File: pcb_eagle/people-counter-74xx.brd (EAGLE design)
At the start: 30.5 x 68.2 mm, 13 parts, among them IC1 74LS90N, IC2 74LS47N

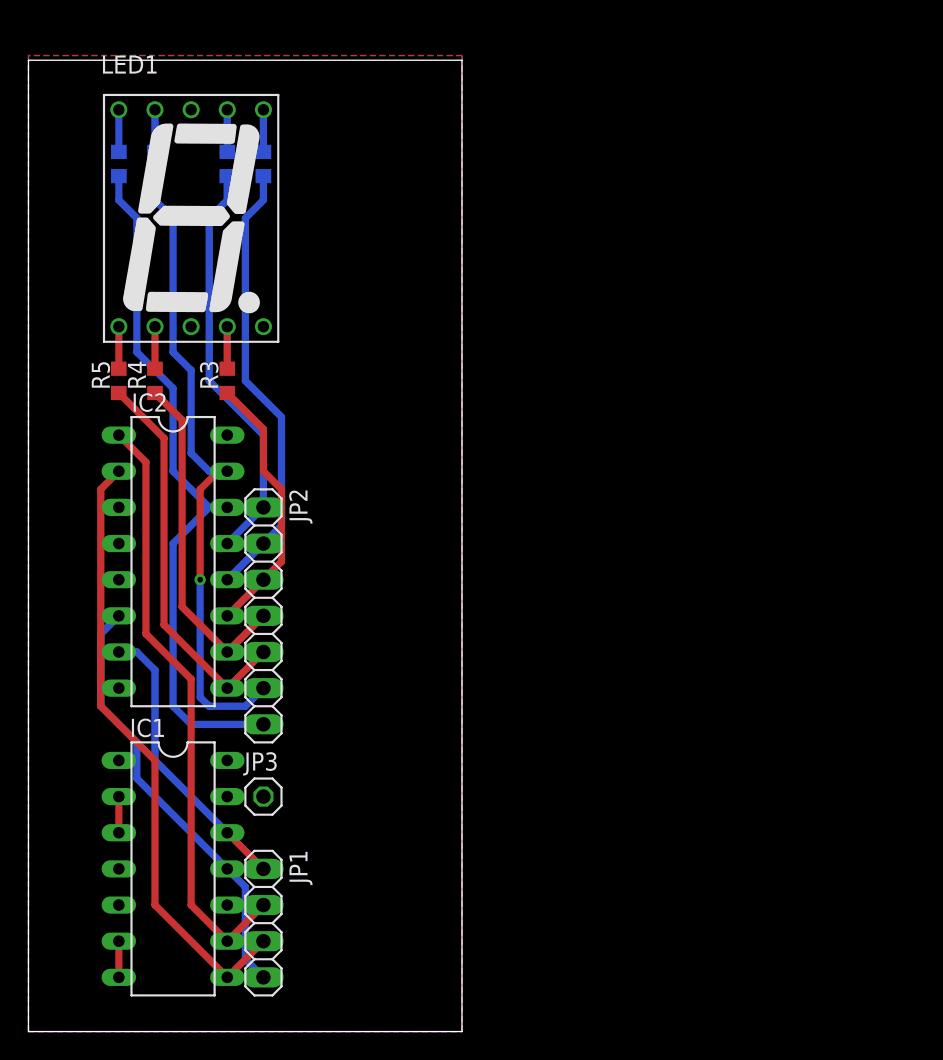
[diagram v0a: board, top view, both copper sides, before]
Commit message: PCB_EAGLE: finish layout of 4 design module (LED segment counter}
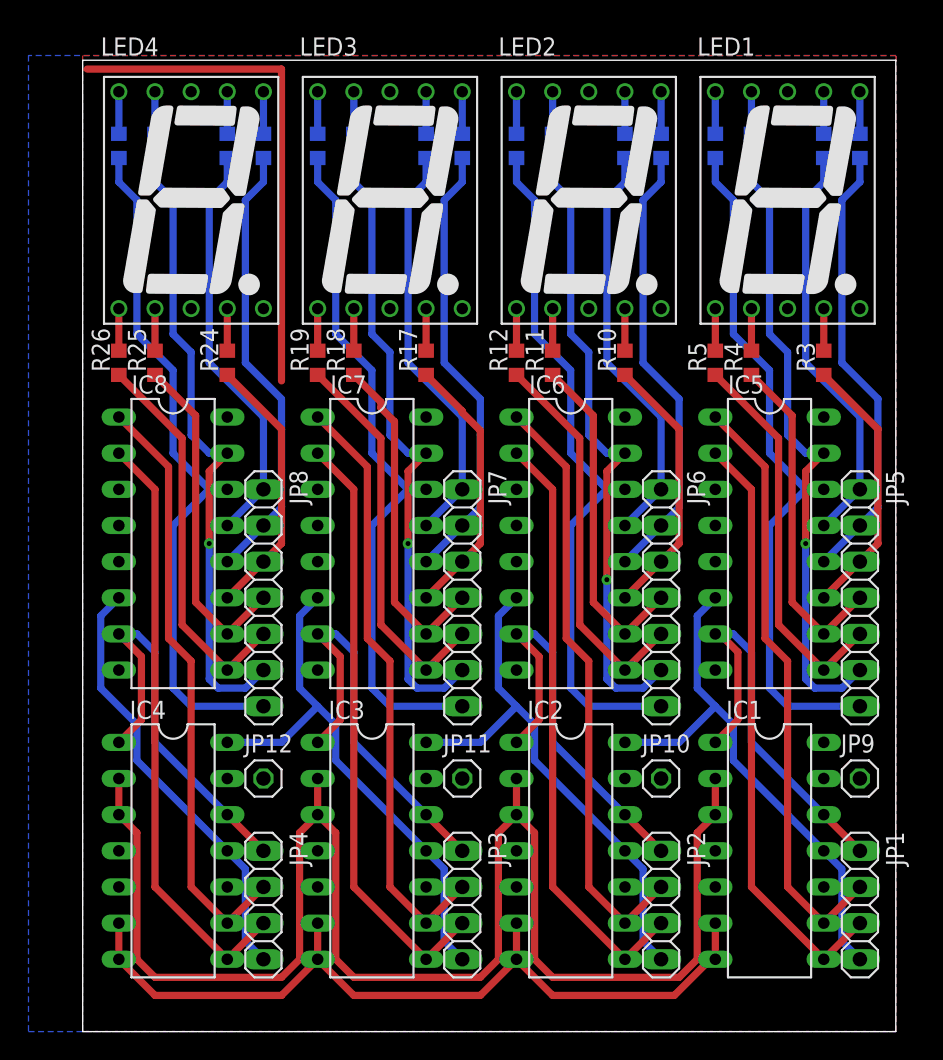
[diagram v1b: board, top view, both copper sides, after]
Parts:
- added IC3, IC4: 74LS90N, 74xx-eu:DIL14
- added IC5, IC6, IC7, IC8: 74LS47N, 74xx-eu:DIL16
- added JP10, JP11, JP12, JP9: GND, pinhead:1X01
- added JP4: NUM4, pinhead:1X04
- added JP5: DIG1, pinhead:1X07
- added JP6: DIG2, pinhead:1X07
- added JP7: DIG3, pinhead:1X07
- added JP8: DIG4, pinhead:1X07
- added LED2, LED3, LED4: 7-SEG_SA52-11, display-kingbright:SA52-11
- added R10, R11, R12, R13, R14, R15, R16, R17, R18, R19, R20, R21, R22, R23, R24, R25, R26, R27, R28, R8, R9: 220R, rcl:R0603
- IC2: value 74LS47N -> 74LS90N; device 74xx-eu:DIL16 -> 74xx-eu:DIL14
- JP2: value DIG1 -> NUM2; device pinhead:1X07 -> pinhead:1X04
- JP3: value GND -> NUM3; device pinhead:1X01 -> pinhead:1X04
- moved LED1 41.9 mm to (53.3, 58.4)
- moved R1 41.9 mm to (55.9, 62.2)
- moved R3 41.9 mm to (55.9, 47.0)
- moved IC1 41.9 mm to (52.1, 12.7)
- moved JP1 41.9 mm to (58.4, 8.89)
- moved R2 41.9 mm to (58.4, 62.2)
- moved R4 41.9 mm to (50.8, 47.0)
- moved R5 41.9 mm to (48.3, 47.0)
- moved R6 41.9 mm to (50.8, 62.2)
- moved R7 41.9 mm to (48.3, 62.2)
- moved IC2 34.5 mm to (38.1, 12.7)
- moved JP2 34.5 mm to (44.5, 8.89)
- moved JP3 15.9 mm to (30.5, 8.89), turned to 270 degrees
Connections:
- removed net CKB_DIG1: IC1.1
- removed net R0_DIG1: IC1.2, IC1.3
- removed net R9_DIG1: IC1.6, IC1.7
- new net A_DIG2: IC6.13, JP6.1, R8.1
- new net A_DIG3: IC7.13, JP7.1, R15.1
- new net A_DIG4: IC8.13, JP8.1, R22.1
- new net A_DIG_2: LED2.7, R8.2
- new net A_DIG_3: LED3.7, R15.2
- new net A_DIG_4: LED4.7, R22.2
- new net B_DIG2: IC6.12, JP6.2, R9.1
- new net B_DIG3: IC7.12, JP7.2, R16.1
- new net B_DIG4: IC8.12, JP8.2, R23.1
- new net B_DIG_2: LED2.6, R9.2
- new net B_DIG_3: LED3.6, R16.2
- new net B_DIG_4: LED4.6, R23.2
- new net C_DIG2: IC6.11, JP6.3, R10.1
- new net C_DIG3: IC7.11, JP7.3, R17.1
- new net C_DIG4: IC8.11, JP8.3, R24.1
- new net C_DIG_2: LED2.4, R10.2
- new net C_DIG_3: LED3.4, R17.2
- new net C_DIG_4: LED4.4, R24.2
- new net D_DIG2: IC6.10, JP6.4, R11.1
- new net D_DIG3: IC7.10, JP7.4, R18.1
- new net D_DIG4: IC8.10, JP8.4, R25.1
- new net D_DIG_2: LED2.2, R11.2
- new net D_DIG_3: LED3.2, R18.2
- new net D_DIG_4: LED4.2, R25.2
- new net E_DIG2: IC6.9, JP6.5, R12.1
- new net E_DIG3: IC7.9, JP7.5, R19.1
- new net E_DIG4: IC8.9, JP8.5, R26.1
- new net E_DIG_2: LED2.1, R12.2
- new net E_DIG_3: LED3.1, R19.2
- new net E_DIG_4: LED4.1, R26.2
- new net F_DIG2: IC6.15, JP6.6, R13.1
- new net F_DIG3: IC7.15, JP7.6, R20.1
- new net F_DIG4: IC8.15, JP8.6, R27.1
- new net F_DIG_2: LED2.9, R13.2
- new net F_DIG_3: LED3.9, R20.2
- new net F_DIG_4: LED4.9, R27.2
- new net G_DIG2: IC6.14, JP6.7, R14.1
- new net G_DIG3: IC7.14, JP7.7, R21.1
- new net G_DIG4: IC8.14, JP8.7, R28.1
- new net G_DIG_2: LED2.10, R14.2
- new net G_DIG_3: LED3.10, R21.2
- new net G_DIG_4: LED4.10, R28.2
- new net QA_IA_DIG2: IC2.1, IC2.12, IC6.7, JP2.1
- new net QA_IA_DIG3: IC3.1, IC3.12, IC7.7, JP3.1
- new net QA_IA_DIG4: IC4.1, IC4.12, IC8.7, JP4.1
- new net QB_IB_DIG2: IC2.9, IC6.1, JP2.2
- new net QB_IB_DIG3: IC3.9, IC7.1, JP3.2
- new net QB_IB_DIG4: IC4.9, IC8.1, JP4.2
- new net QC_IC_DIG2: IC2.8, IC6.2, JP2.3
- new net QC_IC_DIG3: IC3.8, IC7.2, JP3.3
- new net QC_IC_DIG4: IC4.8, IC8.2, JP4.3
- new net QD_ID_DIG2: IC2.11, IC3.14, IC6.6, JP2.4
- new net QD_ID_DIG3: IC3.11, IC4.14, IC7.6, JP3.4
- new net QD_ID_DIG4: IC4.11, IC8.6, JP4.4
- new net R0_DIG: IC1.2, IC1.3, IC2.2, IC2.3, IC3.2, IC3.3, IC4.2, IC4.3
- new net R9_DIG: IC1.6, IC1.7, IC2.6, IC2.7, IC3.6, IC3.7, IC4.6, IC4.7
- net A_DIG1: now also IC5.13, JP5.1; no longer IC2.13, JP2.1
- net B_DIG1: now also IC5.12, JP5.2; no longer IC2.12, JP2.2
- net C_DIG1: now also IC5.11, JP5.3; no longer IC2.11, JP2.3
- net D_DIG1: now also IC5.10, JP5.4; no longer IC2.10, JP2.4
- net E_DIG1: now also IC5.9, JP5.5; no longer IC2.9, JP2.5
- net F_DIG1: now also IC5.15, JP5.6; no longer IC2.15, JP2.6
- net GND: now also IC2.10, IC3.10, IC4.10, IC5.8, IC6.8, IC7.8, IC8.8, JP10.1, JP11.1, JP12.1, JP9.1; no longer IC2.8, JP3.1
- net G_DIG1: now also IC5.14, JP5.7; no longer IC2.14, JP2.7
- net QA_IA_DIG1: now also IC1.1, IC5.7; no longer IC2.7
- net QB_IB_DIG1: now also IC5.1; no longer IC2.1
- net QC_IC_DIG1: now also IC5.2; no longer IC2.2
- net QD_ID_DIG1: now also IC2.14, IC5.6; no longer IC2.6
- net VCC: now also IC3.5, IC4.5, IC5.16, IC5.3, IC5.4, IC5.5, IC6.16, IC6.3, IC6.4, IC6.5, IC7.16, IC7.3, IC7.4, IC7.5, IC8.16, IC8.3, IC8.4, IC8.5, LED2.3, LED2.5, LED2.8, LED3.3, LED3.5, LED3.8, LED4.3, LED4.5, LED4.8; no longer IC2.16, IC2.3, IC2.4
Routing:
- net R0_DIG: track 0.00 -> 111.7 mm
- net R9_DIG: track 0.00 -> 58.4 mm
- net G_DIG4: track 0.00 -> 49.1 mm
- net G_DIG3: track 0.00 -> 49.1 mm
- net G_DIG2: track 0.00 -> 49.1 mm
- net F_DIG4: track 0.00 -> 44.6 mm, vias 0 -> 1
- net F_DIG3: track 0.00 -> 44.6 mm, vias 0 -> 1
- net F_DIG2: track 0.00 -> 44.6 mm, vias 0 -> 1
- net QC_IC_DIG4: track 0.00 -> 42.3 mm
- net QC_IC_DIG2: track 0.00 -> 42.3 mm
- net QB_IB_DIG4: track 0.00 -> 42.3 mm
- net QB_IB_DIG2: track 0.00 -> 42.3 mm
- net QC_IC_DIG3: track 0.00 -> 42.3 mm
- net QB_IB_DIG3: track 0.00 -> 42.3 mm
- net QD_ID_DIG3: track 0.00 -> 38.1 mm
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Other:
- board size 30.5 x 68.2 mm -> 57.1 x 68.2 mm

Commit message: PCB_EAGLE: add frequency square wave generator based on the NE555 and some connectors to schema
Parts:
- added C1: 10n, rcl:C0603
- added C2, C3: x, rcl:C0603
- added C4: (no value), rcl:E5-10,5
- added IC9: NE555N, linear:DIL08
- added JP13: DETECTOR, pinhead:1X03/90
- added JP14: INPUT_SELECT, pinhead:2X02
- added JP15: POWER, pinhead:1X04/90
- added R29: 1M, rcl:PT-10
- added R30, R31: 500k, rcl:R0603
- added R32: 10k, rcl:R0603
- added S1: RESET, switch-omron:B3F-10XX
- added X1: USB-MICRO-B-BOTTOM, usb:USB-MICRO-B-BOTTOM-MOLEX
- moved R1 12.7 mm to (55.9, 74.9)
- moved R13 12.7 mm to (36.8, 74.9)
- moved R14 12.7 mm to (34.3, 74.9)
- moved R15 12.7 mm to (27.9, 74.9)
- moved R16 12.7 mm to (30.5, 74.9)
- moved R2 12.7 mm to (58.4, 74.9)
- moved R20 12.7 mm to (22.9, 74.9)
- moved R21 12.7 mm to (20.3, 74.9)
- moved R22 12.7 mm to (14.0, 74.9)
- moved R23 12.7 mm to (16.5, 74.9)
- moved R27 12.7 mm to (8.89, 74.9)
- moved R28 12.7 mm to (6.35, 74.9)
- moved R6 12.7 mm to (50.8, 74.9)
- moved R7 12.7 mm to (48.3, 74.9)
- moved R8 12.7 mm to (41.9, 74.9)
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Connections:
- removed net R0_DIG: IC1.2, IC1.3, IC2.2, IC2.3, IC3.2, IC3.3, IC4.2, IC4.3
- new net GENERATOR: IC9.3, JP14.1
- new net N$2: R29.2, R31.1
- new net N$3: C2.1, IC9.2, IC9.6, R29.3
- new net N$4: C1.2, IC9.5
- new net N$5: JP13.2, JP14.3
- new net N$6: IC9.7, R30.1, R31.2
- net CKA_DIG1: now also JP14.2, JP14.4
- net GND: now also C1.1, C2.2, C4.-, IC1.2, IC1.3, IC2.2, IC2.3, IC3.2, IC3.3, IC4.2, IC4.3, IC9.1, JP13.3, JP15.3, JP15.4, R29.1, R32.1, X1.5
- net R9_DIG: now also C3.2, R32.2, S1.1, S1.2
- net VCC: now also C3.1, C4.+, IC9.4, IC9.8, JP13.1, JP15.1, JP15.2, R30.2, S1.3, S1.4, X1.1
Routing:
- net R0_DIG: track 111.7 -> 0.00 mm
- net GND: track 0.00 -> 111.7 mm
- net N$1: track 35.6 -> 0.00 mm
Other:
- board size 57.1 x 68.2 mm -> 74.9 x 81 mm

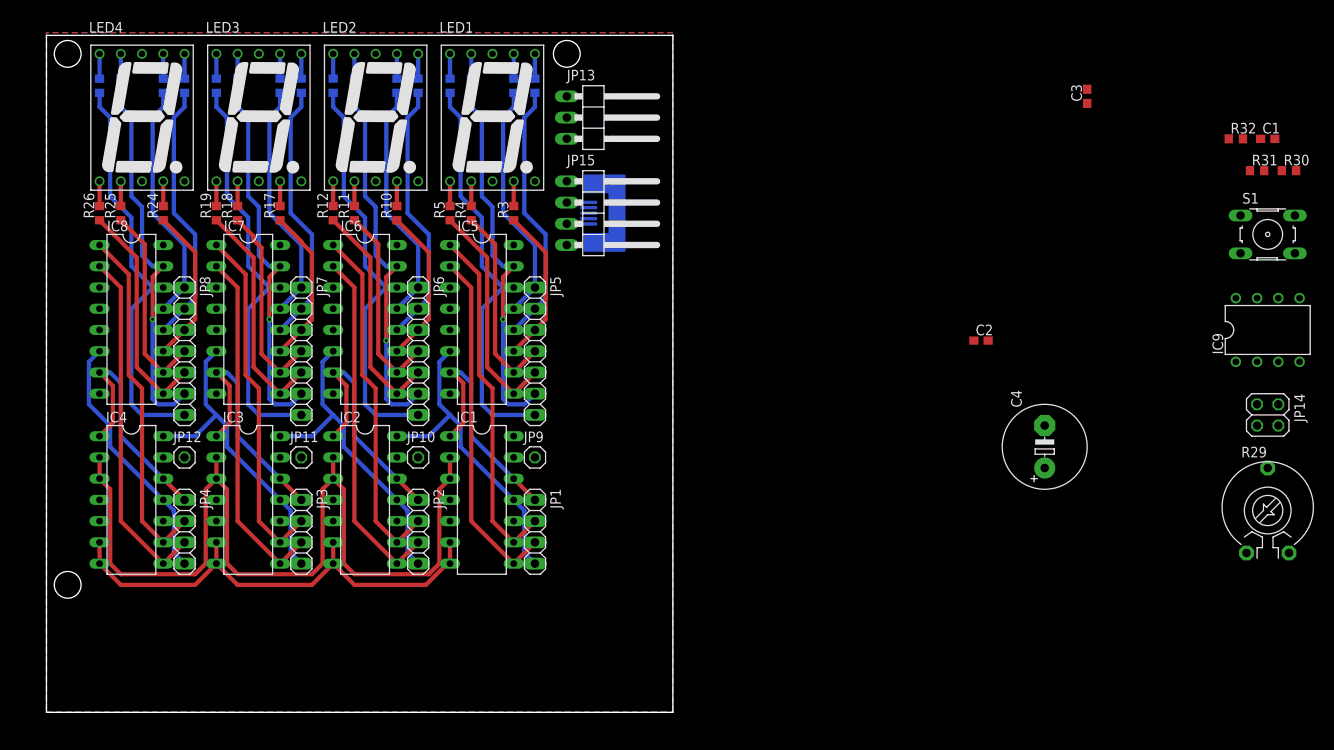
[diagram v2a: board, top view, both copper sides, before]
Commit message: PCB_EAGLE: final layout of board
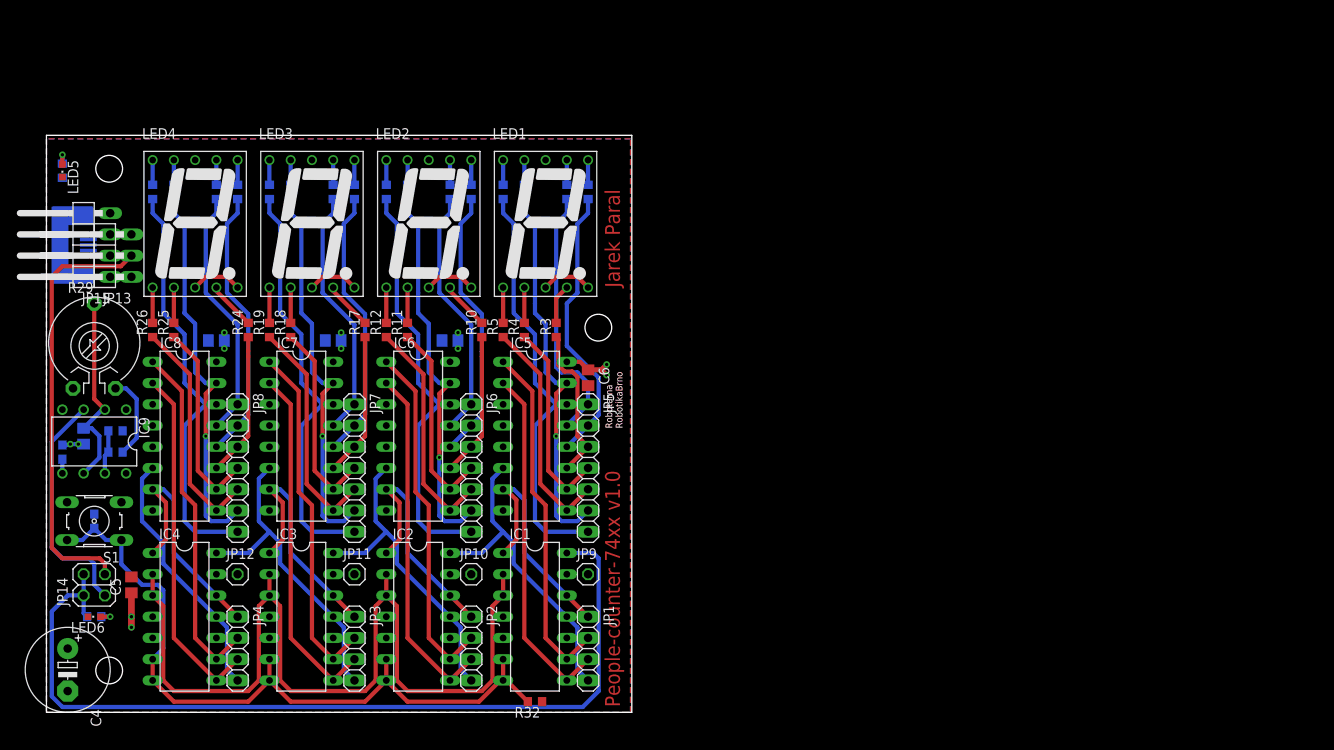
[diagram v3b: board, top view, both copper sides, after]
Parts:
- added C5, C6, C7, C8, C9: 10u, rcl:C0805
- added LED5: green, led:CHIPLED_0603
- added LED6: red, led:CHIPLED_0603
- added R33, R34: 220R, rcl:R0603
- C2: value x -> 10u; device rcl:C0603 -> rcl:C0805
- C3: value x -> 10n
- C4: value (none) -> 1m
- moved C1 148.9 mm to (1.91, 31.1), flipped to the bottom, turned to 270 degrees
- moved S1 144.5 mm to (5.71, 22.9), turned to 180 degrees
- moved R30 143.7 mm to (8.26, 33.7), flipped to the bottom, turned to 180 degrees
- moved JP14 141.8 mm to (5.71, 15.2), turned to 90 degrees
- moved R29 141.7 mm to (5.71, 43.8)
- moved IC9 141.0 mm to (5.71, 32.4), turned to 180 degrees
- moved R31 140.6 mm to (8.26, 31.1), flipped to the bottom
- moved C3 129.2 mm to (5.71, 22.9), flipped to the bottom, turned to 270 degrees
- moved C4 119.8 mm to (2.54, 5.08), turned to 270 degrees
- moved C2 107.9 mm to (4.45, 33.0), flipped to the bottom, turned to 270 degrees
- moved R32 107.5 mm to (58.4, 1.27), turned to 180 degrees
- moved X1 70.0 mm to (0.00, 55.9), turned to 180 degrees
- moved JP15 62.3 mm to (3.81, 55.9), turned to 90 degrees
- moved JP13 61.9 mm to (6.35, 54.6), turned to 90 degrees
- moved R10 17.3 mm to (52.1, 45.7)
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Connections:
- new net +5V: R33.2
- new net N$1: LED6.A, R34.1
- new net N$11: LED5.A, R33.1
- net CKA_DIG1: now also R34.2
- net GND: now also C5.2, C6.2, C7.2, C8.2, C9.2, LED5.C, LED6.C
- net VCC: now also C5.1, C6.1, C7.1, C8.1, C9.1
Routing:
- net CKA_DIG1: track 0.00 -> 106.7 mm
- net N$5: track 0.00 -> 51.4 mm
- net VCC: track 0.00 -> 37.7 mm, vias 0 -> 4
- net R9_DIG: track 58.4 -> 88.0 mm
- net GENERATOR: track 0.00 -> 28.3 mm
- net N$3: track 0.00 -> 24.2 mm
- net GND: track 111.7 -> 122.7 mm, vias 0 -> 8
- net N$2: track 0.00 -> 10.1 mm
- net N$6: track 0.00 -> 5.25 mm
- net C_DIG_3: track 2.96 -> 5.81 mm
- net C_DIG_2: track 2.96 -> 5.81 mm
- net C_DIG_4: track 2.96 -> 5.81 mm
- net A_DIG1: track 29.0 -> 31.4 mm
- net B_DIG1: track 31.5 -> 33.8 mm
- net N$1: track 0.00 -> 2.21 mm, vias 0 -> 1
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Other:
- board size 74.9 x 81 mm -> 70 x 69 mm
- board text added: "CC BY-SA 4.0"
- board text added: "Jarek Paral"
- board text added: "People-counter-74xx v1.0"
- board text added: "Robotarna RobotikaBrno"

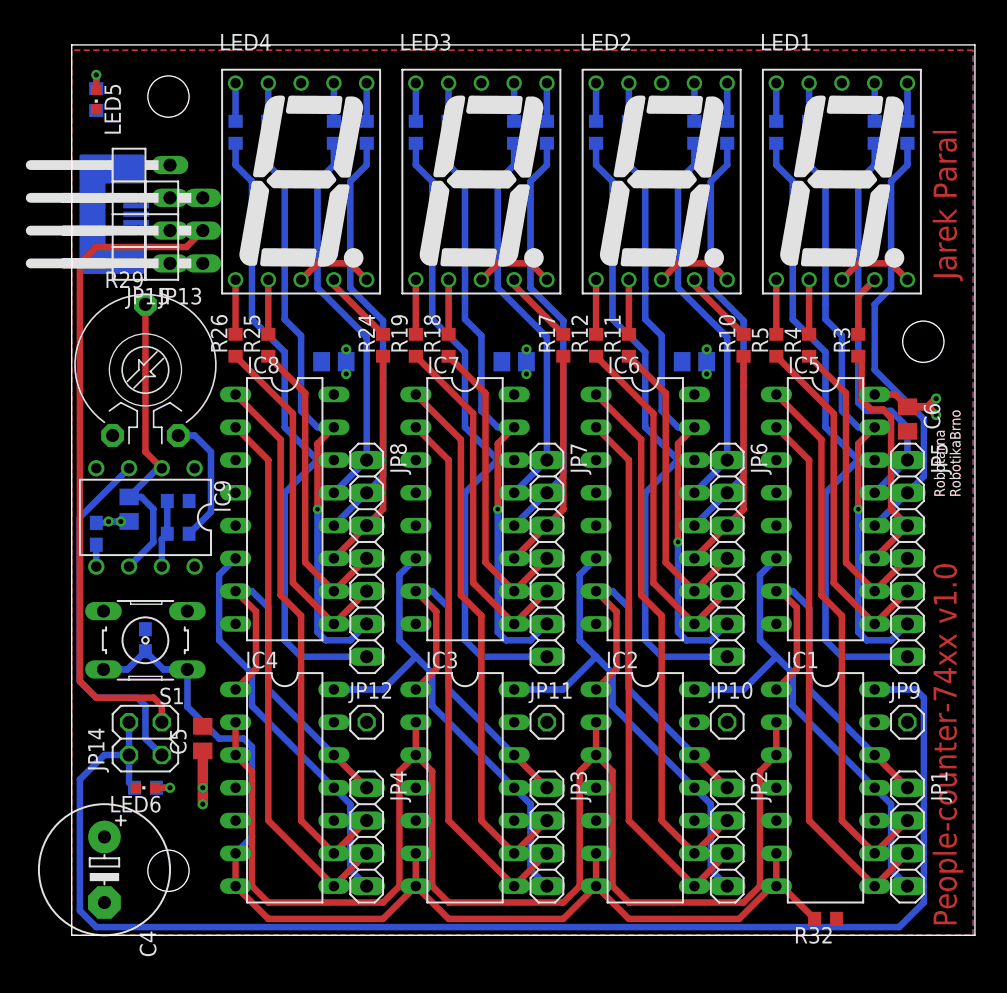
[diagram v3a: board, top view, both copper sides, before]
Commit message: PCB_EAGLE: add a few description text and some optimization of net
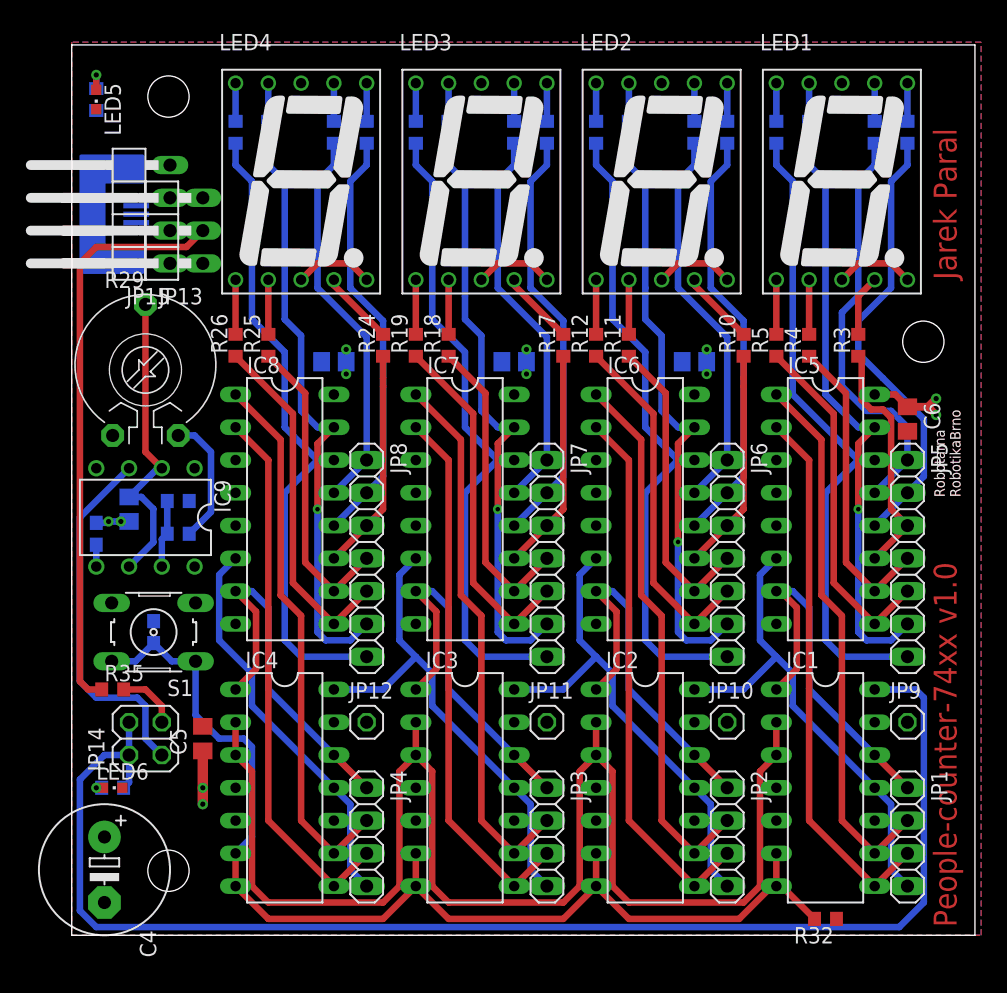
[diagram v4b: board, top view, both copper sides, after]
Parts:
- added R35: 220R, rcl:R0603
- moved LED6 2.54 mm to (3.17, 11.4), turned to 270 degrees
- moved R34 2.54 mm to (3.17, 11.4), turned to 180 degrees
- moved C3 0.90 mm to (6.35, 23.5)
- moved S1 0.90 mm to (6.35, 23.5)
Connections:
- removed net N$5: JP13.2, JP14.3
- new net SIGNAL_INPUT: JP13.2, R35.1
- new net SIGNAL_INPUT_: JP14.3, R35.2
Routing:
- net N$5: track 51.4 -> 0.00 mm
- net SIGNAL_INPUT: track 0.00 -> 45.1 mm
- net SIGNAL_INPUT_: track 0.00 -> 4.76 mm
- net N$1: track 2.21 -> 0.94 mm
- net A_DIG1: track 31.4 -> 32.4 mm
- net B_DIG1: track 33.8 -> 34.9 mm
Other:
- board text added: "+"
- board text added: "+5V"
- board text added: "-"
- board text added: "GEN"
- board text added: "GND"
- board text added: "INP"
- board text added: "ON"
- board text added: "RESET"
- board text added: "S"
- board text added: "SIG"
